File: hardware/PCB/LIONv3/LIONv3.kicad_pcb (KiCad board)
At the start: 2 copper layers, 45 x 45 mm, 52 parts, among them J1 Conn_01x14, U1 TPS259474ARPWR, U14 E80-900M2213S, U2 ESP32-C6-MINI-1-N4, U3 TPS259472ARPWR, U4 TLV75533PDQNR, U5 TCAN3414DR, U6 TMP112AIDRLR, U7 INA226AIDGSR, U9 INA226AIDGSR

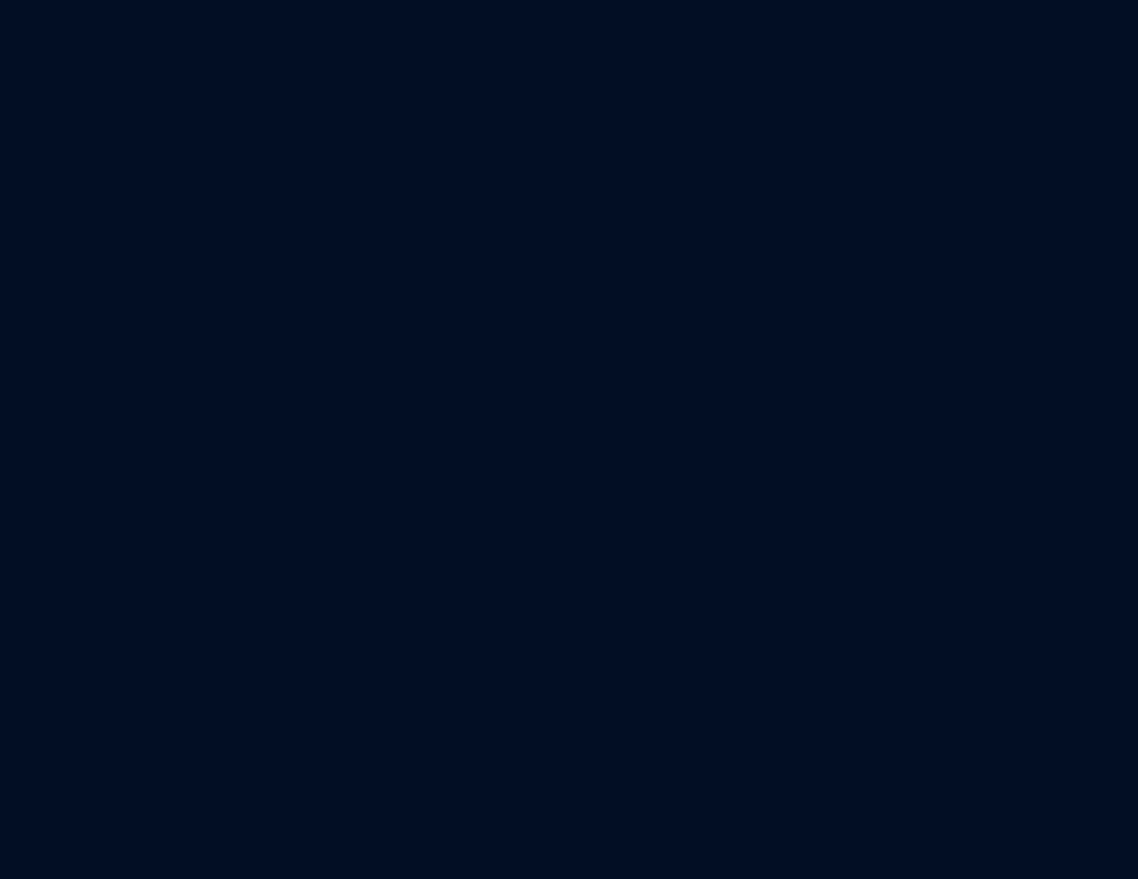
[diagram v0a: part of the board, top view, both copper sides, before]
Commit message: feat(hardware): organize schematic pages
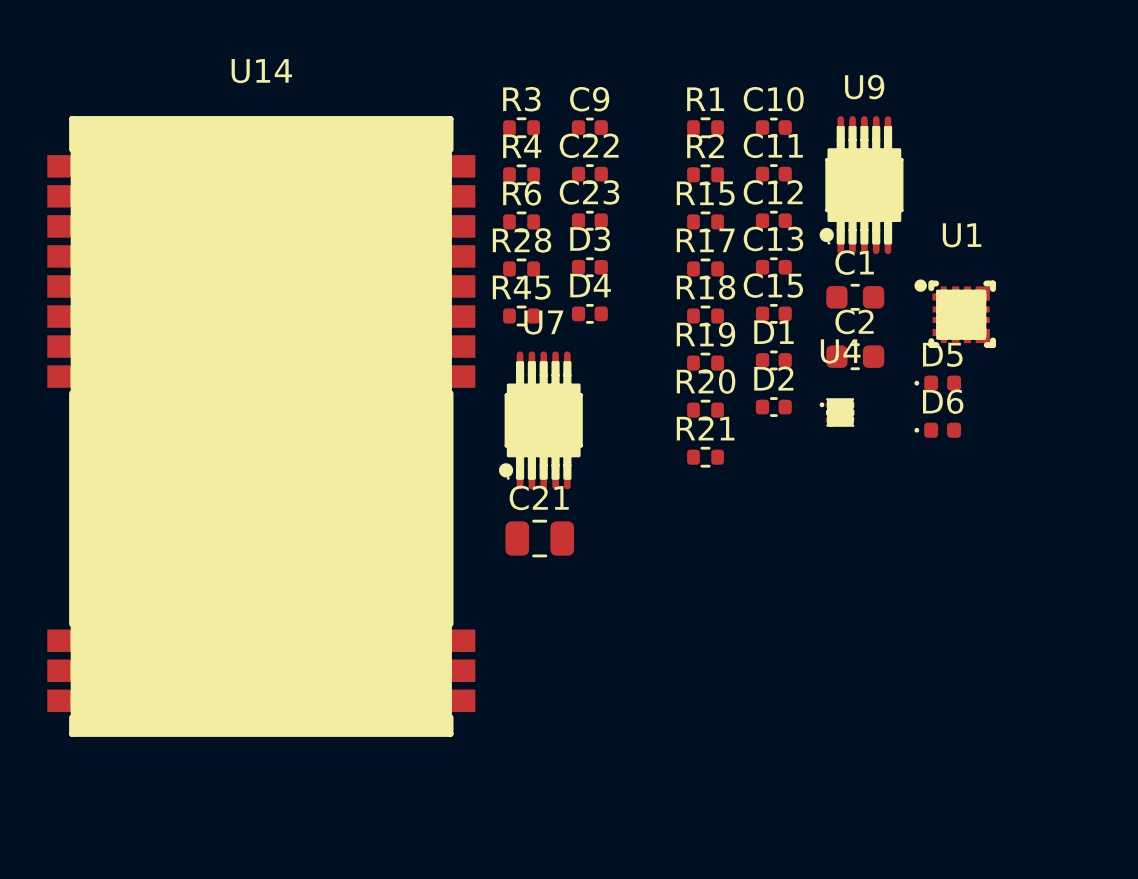
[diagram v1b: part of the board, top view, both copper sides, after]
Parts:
- added C1: 1uF, Capacitor_SMD:C_0603_1608Metric, F.Cu at (34.7, 7.67)
- added C10: 100nF, Capacitor_SMD:C_0402_1005Metric, F.Cu at (31.3, 0.48)
- added C11: 1uF, Capacitor_SMD:C_0402_1005Metric, F.Cu at (31.3, 2.46)
- added C12: 3.3nF, Capacitor_SMD:C_0402_1005Metric, F.Cu at (31.3, 4.42)
- added C13: 2.2nF, Capacitor_SMD:C_0402_1005Metric, F.Cu at (31.3, 6.39)
- added C15: 1uF, Capacitor_SMD:C_0402_1005Metric, F.Cu at (31.3, 8.37)
- added C2: 1uF, Capacitor_SMD:C_0603_1608Metric, F.Cu at (34.7, 10.2)
- added C21: 22uF, Capacitor_SMD:C_0805_2012Metric, F.Cu at (21.4, 17.9)
- added C22: 100nF, Capacitor_SMD:C_0402_1005Metric, F.Cu at (23.5, 2.46)
- added C23: 100nF, Capacitor_SMD:C_0402_1005Metric, F.Cu at (23.5, 4.42)
- added C9: 100nF, Capacitor_SMD:C_0402_1005Metric, F.Cu at (23.5, 0.48)
- added D1: LED, Capacitor_SMD:C_0402_1005Metric, F.Cu at (31.3, 10.3)
- added D2: LED, Capacitor_SMD:C_0402_1005Metric, F.Cu at (31.3, 12.3)
- added D3: LED, Capacitor_SMD:C_0402_1005Metric, F.Cu at (23.5, 6.39)
- added D4: LED, Capacitor_SMD:C_0402_1005Metric, F.Cu at (23.5, 8.37)
- added D5: D_Schottky, Diode_SMD:D_0402_1005Metric, F.Cu at (38.4, 11.3)
- added D6: D_Schottky, Diode_SMD:D_0402_1005Metric, F.Cu at (38.4, 13.3)
- added R1: 1k, Resistor_SMD:R_0402_1005Metric, F.Cu at (28.4, 0.49)
- added R15: 10k, Resistor_SMD:R_0402_1005Metric, F.Cu at (28.4, 4.47)
- added R17: 133k, Resistor_SMD:R_0402_1005Metric, F.Cu at (28.4, 6.46)
- added R18: 100k, Resistor_SMD:R_0402_1005Metric, F.Cu at (28.4, 8.46)
- added R19: 6.65k, Resistor_SMD:R_0402_1005Metric, F.Cu at (28.4, 10.4)
- added R2: 1k, Resistor_SMD:R_0402_1005Metric, F.Cu at (28.4, 2.48)
- added R20: 15k, Resistor_SMD:R_0402_1005Metric, F.Cu at (28.4, 12.4)
- added R21: 10k, Resistor_SMD:R_0402_1005Metric, F.Cu at (28.4, 14.4)
- added R28: 10k, Resistor_SMD:R_0402_1005Metric, F.Cu at (20.6, 6.46)
- added R3: 1k, Resistor_SMD:R_0402_1005Metric, F.Cu at (20.6, 0.49)
- added R4: 1k, Resistor_SMD:R_0402_1005Metric, F.Cu at (20.6, 2.48)
- added R45: 10k, Resistor_SMD:R_0402_1005Metric, F.Cu at (20.6, 8.46)
- added R6: 10k, Resistor_SMD:R_0402_1005Metric, F.Cu at (20.6, 4.47)
- added U1: TPS259474ARPWR, LIONv3-Footprints:VQFN-10_L2.0-W2.0-P0.45-TL, F.Cu at (39.2, 8.40)
- added U14: E80-900M2213S, LIONv3-Footprints:WIFIM-SMD_22P-L26.0-W16.0-P1.27-TL, F.Cu at (9.59, 13.4)
- added U4: TLV75533PDQNR, LIONv3-Footprints:X2SON-4_L1.0-W1.0-P0.65-TL-EP, F.Cu at (34.1, 12.5)
- added U7: INA226AIDGSR, LIONv3-Footprints:MSOP-10_L3.0-W3.0-P0.50-LS5.0-BL, F.Cu at (21.5, 12.9)
- added U9: INA226AIDGSR, LIONv3-Footprints:MSOP-10_L3.0-W3.0-P0.50-LS5.0-BL, F.Cu at (35.1, 2.92)
- R12, R13: value 60.4 -> 61

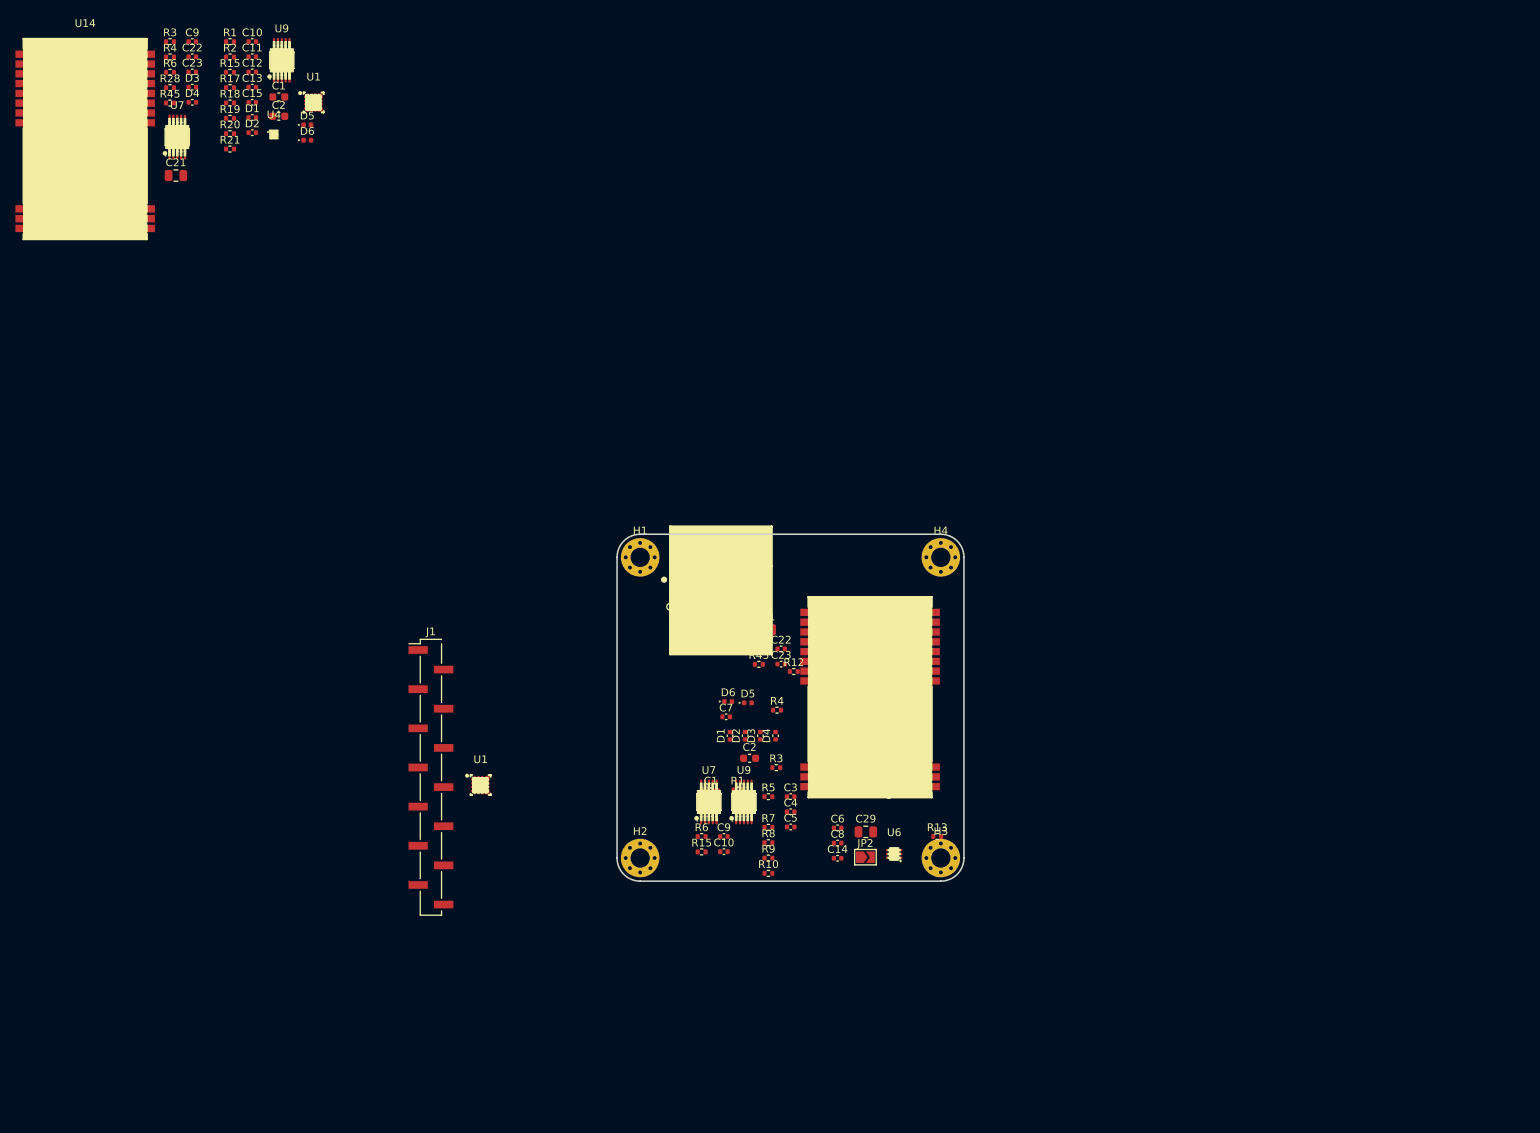
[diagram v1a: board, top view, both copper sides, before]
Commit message: feat(hardware): finish ESP32-C6 electrical schematic
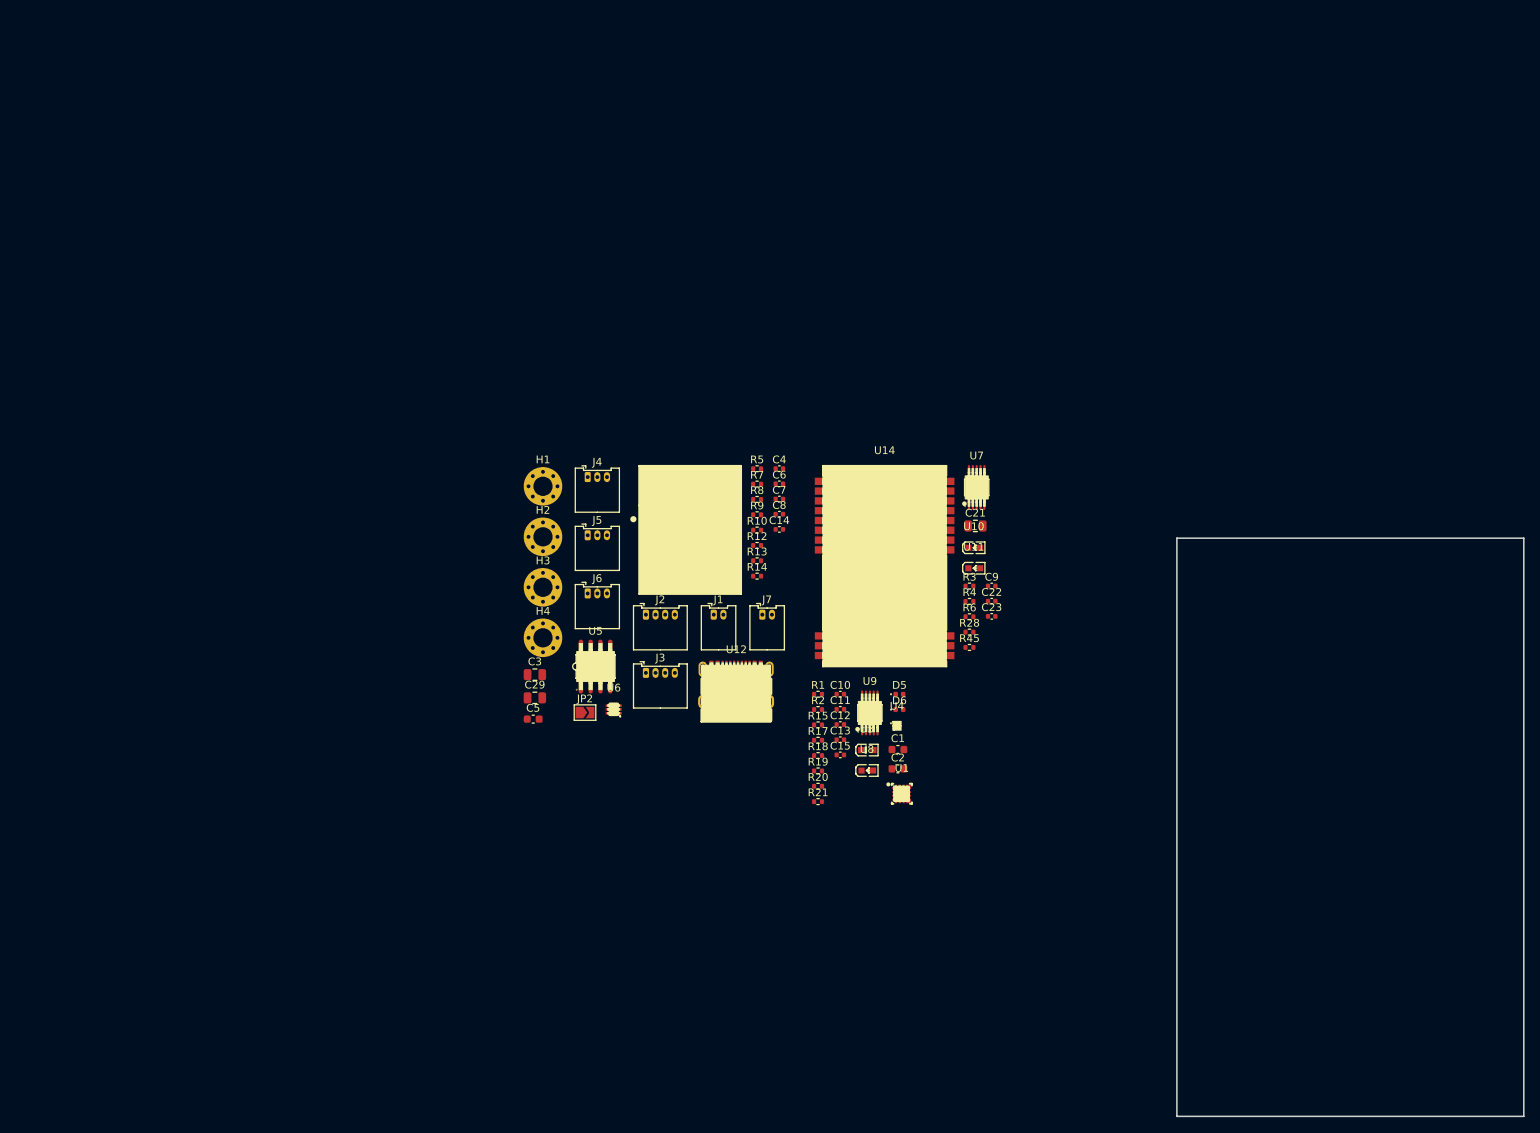
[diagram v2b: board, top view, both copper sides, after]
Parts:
- removed the C1 at (34.7, 7.67)
- removed the C1 at (90.7, 97.8)
- removed the C10 at (31.3, 0.48)
- removed the C10 at (92.4, 105.6)
- removed the C2 at (95.8, 93.5)
- removed the C2 at (34.7, 10.2)
- removed the C21 at (21.4, 17.9)
- removed the C21 at (97.8, 76.8)
- removed the C22 at (23.5, 2.46)
- removed the C22 at (99.9, 79.3)
- removed the C23 at (23.5, 4.42)
- removed the C23 at (99.9, 81.2)
- removed the C9 at (23.5, 0.48)
- removed the C9 at (92.4, 103.6)
- removed D1 (x2), D2 (x2), D3 (x2), D4 (x2): LED, Capacitor_SMD:C_0402_1005Metric
- removed the D5 at (95.6, 86.3)
- removed the D5 at (38.4, 11.3)
- removed the D6 at (93.0, 86.1)
- removed the D6 at (38.4, 13.3)
- removed the R1 at (94.2, 97.6)
- removed the R1 at (28.4, 0.49)
- removed the R15 at (28.4, 4.47)
- removed the R15 at (89.6, 105.6)
- removed the R2 at (28.4, 2.48)
- removed the R2 at (94.2, 99.5)
- removed the R28 at (20.6, 6.46)
- removed the R28 at (97.0, 79.3)
- removed the R3 at (99.2, 94.7)
- removed the R3 at (20.6, 0.49)
- removed the R4 at (20.6, 2.48)
- removed the R4 at (99.3, 87.2)
- removed the R45 at (97.0, 81.3)
- removed the R45 at (20.6, 8.46)
- removed the R6 at (89.6, 103.6)
- removed the R6 at (20.6, 4.47)
- removed the U1 at (39.2, 8.40)
- removed the U1 at (60.8, 96.9)
- removed the U14 at (9.59, 13.4)
- removed the U14 at (111.4, 85.8)
- removed the U4 at (88.6, 76.5)
- removed the U4 at (34.1, 12.5)
- removed the U7 at (90.5, 99.1)
- removed the U7 at (21.5, 12.9)
- removed the U9 at (95.0, 99.1)
- removed the U9 at (35.1, 2.92)
- added C1: 1uF, Capacitor_SMD:C_0603_1608Metric, F.Cu at (115.0, 92.3)
- added C10: 100nF, Capacitor_SMD:C_0402_1005Metric, F.Cu at (107.5, 85.1)
- added C2: 1uF, Capacitor_SMD:C_0603_1608Metric, F.Cu at (115.0, 94.8)
- added C21: 22uF, Capacitor_SMD:C_0805_2012Metric, F.Cu at (125.1, 63.3)
- added C22: 100nF, Capacitor_SMD:C_0402_1005Metric, F.Cu at (127.2, 73.1)
- added C23: 100nF, Capacitor_SMD:C_0402_1005Metric, F.Cu at (127.2, 75.0)
- added C9: 100nF, Capacitor_SMD:C_0402_1005Metric, F.Cu at (127.2, 71.1)
- added D5: D_Schottky, Diode_SMD:D_0402_1005Metric, F.Cu at (115.2, 85.1)
- added D6: D_Schottky, Diode_SMD:D_0402_1005Metric, F.Cu at (115.2, 87.1)
- added J2: UART, Connector_Molex:Molex_PicoBlade_53048-0410_1x04_P1.25mm_Horizontal, F.Cu at (82.3, 74.8)
- added J3: JTAG, Connector_Molex:Molex_PicoBlade_53048-0410_1x04_P1.25mm_Horizontal, F.Cu at (82.3, 82.4)
- added J4: PWR_GND, Connector_Molex:Molex_PicoBlade_53048-0310_1x03_P1.25mm_Horizontal, F.Cu at (74.8, 57.0)
- added J5: PWR_3.3V, Connector_Molex:Molex_PicoBlade_53048-0310_1x03_P1.25mm_Horizontal, F.Cu at (74.8, 64.5)
- added J6: PWR_5V, Connector_Molex:Molex_PicoBlade_53048-0310_1x03_P1.25mm_Horizontal, F.Cu at (74.8, 72.1)
- added J7: I2C, Connector_Molex:Molex_PicoBlade_53048-0210_1x02_P1.25mm_Horizontal, F.Cu at (97.4, 74.8)
- added R1: 150, Resistor_SMD:R_0402_1005Metric, F.Cu at (104.7, 85.1)
- added R15: 10k, Resistor_SMD:R_0402_1005Metric, F.Cu at (104.7, 89.1)
- added R2: 82, Resistor_SMD:R_0402_1005Metric, F.Cu at (104.7, 87.1)
- added R28: 10k, Resistor_SMD:R_0402_1005Metric, F.Cu at (124.3, 77.1)
- added R3: 68, Resistor_SMD:R_0402_1005Metric, F.Cu at (124.3, 71.1)
- added R4: 68, Resistor_SMD:R_0402_1005Metric, F.Cu at (124.3, 73.1)
- added R45: 10k, Resistor_SMD:R_0402_1005Metric, F.Cu at (124.3, 79.1)
- added R6: 10k, Resistor_SMD:R_0402_1005Metric, F.Cu at (124.3, 75.1)
- added U1: TPS259474ARPWR, LIONv3-Footprints:VQFN-10_L2.0-W2.0-P0.45-TL, F.Cu at (115.5, 98.1)
- added U10: XL-1608UBC-04, LIONv3-Footprints:LED0603-RD_BLUE, F.Cu at (124.9, 66.2)
- added U11: XL-1608UBC-04, LIONv3-Footprints:LED0603-RD_BLUE, F.Cu at (124.9, 68.8)
- added U12: TYPE-C_16PIN_2MD(073), LIONv3-Footprints:USB-C-SMD_TYPE-C-16PIN-2MD-073, F.Cu at (94.0, 83.7)
- added U14: E80-900M2213S, LIONv3-Footprints:WIFIM-SMD_22P-L26.0-W16.0-P1.27-TL, F.Cu at (113.3, 68.8)
- added U4: TLV75533PDQNR, LIONv3-Footprints:X2SON-4_L1.0-W1.0-P0.65-TL-EP, F.Cu at (114.9, 89.2)
- added U7: INA226AIDGSR, LIONv3-Footprints:MSOP-10_L3.0-W3.0-P0.50-LS5.0-BL, F.Cu at (125.2, 58.3)
- added U8: XL-1608SURC-06, LIONv3-Footprints:LED0603-RD_RED, F.Cu at (111.0, 95.0)
- added U9: INA226AIDGSR, LIONv3-Footprints:MSOP-10_L3.0-W3.0-P0.50-LS5.0-BL, F.Cu at (111.4, 87.6)
- C3: value 3.3nF -> 22uF; footprint Capacitor_SMD:C_0402_1005Metric -> Capacitor_SMD:C_0805_2012Metric
- C4: value 2.2nF -> 100nF
- C5: footprint Capacitor_SMD:C_0402_1005Metric -> Capacitor_SMD:C_0603_1608Metric
- C7: value 1uF -> 100nF
- J1: value Conn_01x14 -> CAN; footprint Connector_PinHeader_2.54mm:PinHeader_1x14_P2.54mm_Vertical_SMD_Pin1Left -> Connector_Molex:Molex_PicoBlade_53048-0210_1x02_P1.25mm_Horizontal
- R10: value 10k -> 5.1k
- R5: value 133k -> 10k
- R7: value 100k -> 0
- R8: value 6.65k -> 10k
- R9: value 15k -> 5.1k
- U3: value TPS259472ARPWR -> XL-1608UGC-04; footprint LIONv3-Footprints:VQFN-10_L2.0-W2.0-P0.45-TL -> LIONv3-Footprints:LED0603-RD_GREEN
- moved C11 113.9 mm to (107.5, 87.1)
- moved C12 113.9 mm to (107.5, 89.1)
- moved C13 113.9 mm to (107.5, 91.0)
- moved C15 113.9 mm to (107.5, 93.0)
- moved R18 113.9 mm to (104.7, 93.1)
- moved R19 113.9 mm to (104.7, 95.1)
- moved R21 113.9 mm to (104.7, 99.1)
- moved R17 113.9 mm to (104.7, 91.1)
- moved R20 113.9 mm to (104.7, 97.1)
- moved H3 62.4 mm to (69.0, 71.3)
- moved H4 52.6 mm to (69.0, 77.8)
- moved C29 46.3 mm to (67.9, 85.6)
- moved C6 45.3 mm to (99.6, 57.9)
- moved R10 44.6 mm to (96.7, 63.9)
- moved R7 44.6 mm to (96.7, 57.9)
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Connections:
- C3 pad 1: Net-(U3-ITIMER) -> +3V3
- C4 pad 1: Net-(U3-DVDT) -> +3V3
- C5 pad 1: +3.3V -> Net-(U2-EN)
- C7 pad 1: /3V3_IN -> Net-(C7-Pad1)
- R10 pad 1: Net-(U3-FLT#/PGTH) -> Net-(U12-CC2)
- R5 pad 1: /3V3_IN -> +3V3
- R5 pad 2: Net-(U3-EN/UVLO) -> Net-(U2-EN)
- R7 pad 1: Net-(U3-EN/UVLO) -> Net-(C7-Pad1)
- R7 pad 2: GND -> Net-(U2-EN)
- R8 pad 1: Net-(U3-ILM) -> +3.3V
- R8 pad 2: GND -> /IO8
- R9 pad 1: +3.3V -> Net-(U12-CC1)
- R9 pad 2: Net-(U3-FLT#/PGTH) -> GND
- U2 pad 1: unconnected-(U2-GND-Pad1) -> GND
- U2 pad 10: unconnected-(U2-IO5-Pad10) -> /TDI
- U2 pad 11: unconnected-(U2-GND-Pad11) -> GND
- U2 pad 14: unconnected-(U2-GND-Pad14) -> GND
- U2 pad 15: unconnected-(U2-IO6-Pad15) -> /TCK
- U2 pad 16: unconnected-(U2-IO7-Pad16) -> /TDO
- U2 pad 17: unconnected-(U2-IO12-Pad17) -> /USB_D-
- U2 pad 18: unconnected-(U2-IO13-Pad18) -> /USB_D+
- U2 pad 2: unconnected-(U2-GND-Pad2) -> GND
- U2 pad 22: unconnected-(U2-IO8-Pad22) -> /IO8
- U2 pad 23: unconnected-(U2-IO9-Pad23) -> /IO9
- U2 pad 3: unconnected-(U2-3V3-Pad3) -> +3V3
- U2 pad 30: unconnected-(U2-RXD0-Pad30) -> /UART_RX0
- U2 pad 31: unconnected-(U2-TXD0-Pad31) -> /UART_TX0
- U2 pad 36: unconnected-(U2-GND-Pad36) -> GND
- U2 pad 37: unconnected-(U2-GND-Pad37) -> GND
- U2 pad 38: unconnected-(U2-GND-Pad38) -> GND
- U2 pad 39: unconnected-(U2-GND-Pad39) -> GND
- U2 pad 40: unconnected-(U2-GND-Pad40) -> GND
- U2 pad 41: unconnected-(U2-GND-Pad41) -> GND
- U2 pad 42: unconnected-(U2-GND-Pad42) -> GND
- U2 pad 43: unconnected-(U2-GND-Pad43) -> GND
- U2 pad 44: unconnected-(U2-GND-Pad44) -> GND
- U2 pad 45: unconnected-(U2-GND-Pad45) -> GND
- U2 pad 46: unconnected-(U2-GND-Pad46) -> GND
- U2 pad 47: unconnected-(U2-GND-Pad47) -> GND
- U2 pad 48: unconnected-(U2-GND-Pad48) -> GND
- U2 pad 49: unconnected-(U2-GND-Pad49) -> GND
- U2 pad 50: unconnected-(U2-GND-Pad50) -> GND
- U2 pad 51: unconnected-(U2-GND-Pad51) -> GND
- U2 pad 52: unconnected-(U2-GND-Pad52) -> GND
- U2 pad 53: unconnected-(U2-GND-Pad53) -> GND
- U2 pad 8: unconnected-(U2-EN-Pad8) -> Net-(U2-EN)
- U2 pad 9: unconnected-(U2-IO4-Pad9) -> /TMS
- U3 pad 1: Net-(U3-EN/UVLO) -> GND
- U3 pad 2: GND -> Net-(U3-A)
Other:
- board size 45 x 45 mm -> 45 x 75 mm
